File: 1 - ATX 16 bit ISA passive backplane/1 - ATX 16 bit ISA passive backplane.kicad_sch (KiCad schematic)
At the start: 18 parts, among them J1 BUS 1, J2 A: Component Side, J22 IE12, J23 IE23, J24 IE34, J25 IE45, J26 IE56, J27 IE67, J28 IE78, J3 B: Back Side, J4 BUS 2, J5 BUS 3, J6 BUS 4, J7 BUS 5, J8 BUS 6, J9 BUS 7

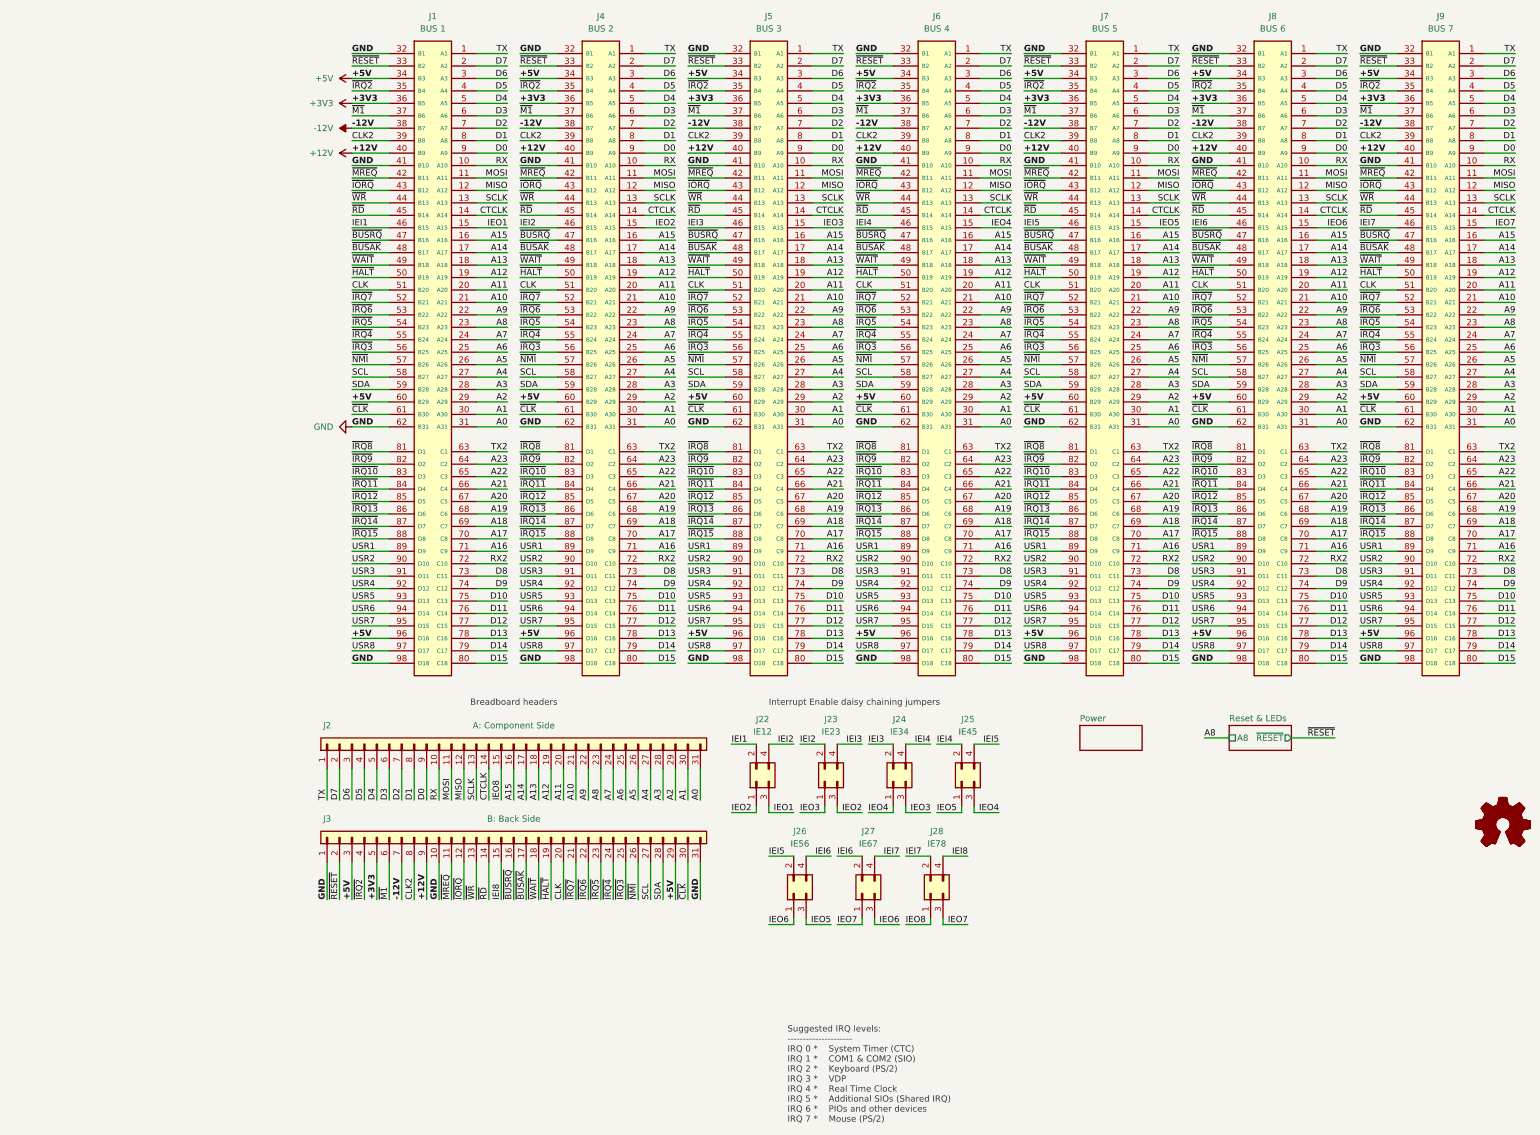
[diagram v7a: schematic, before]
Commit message: Changed lane labeling for IRQ0 and 1
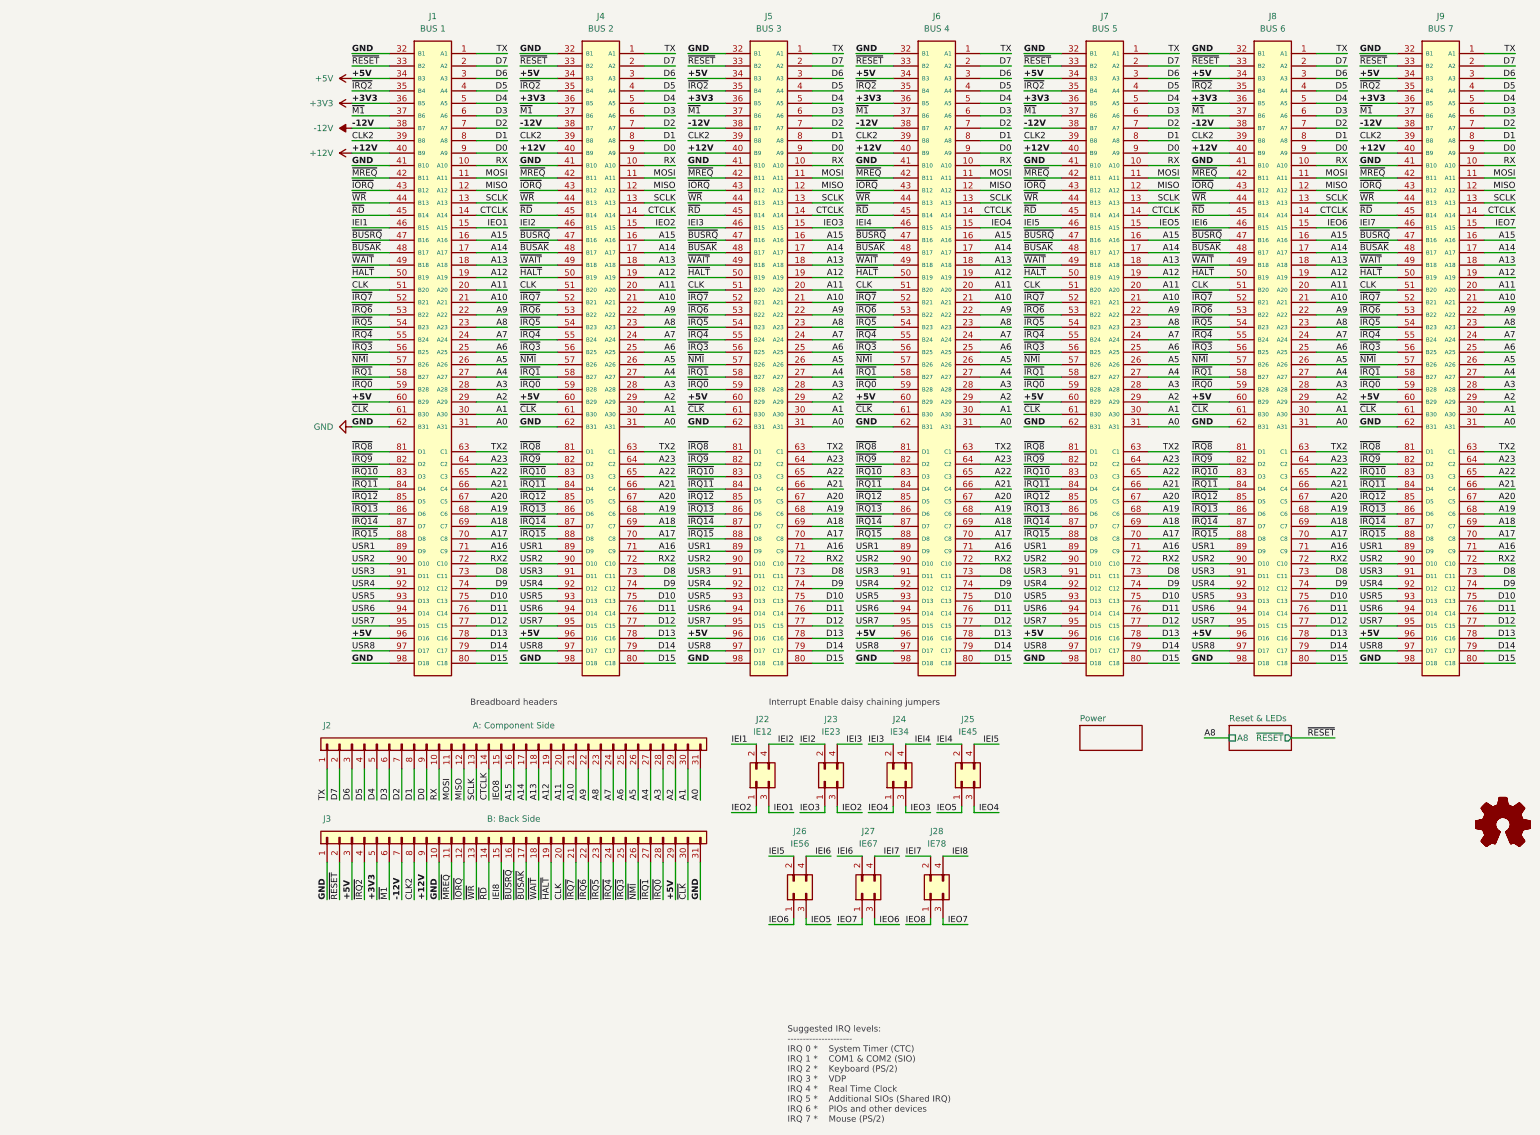
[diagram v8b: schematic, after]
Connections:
- net SCL renamed ~{IRQ1}
- net SDA renamed ~{IRQ0}
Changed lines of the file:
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@@
     (effects (font (size 1.27 1.27)) (justify right bottom))
   )
-  (label "SCL" (at 229.87 88.9 0) (fields_autoplaced)
+  (label "~{IRQ1}" (at 229.87 88.9 0) (fields_autoplaced)
     (effects (font (size 1.27 1.27)) (justify left bottom))
   )
@@
     (effects (font (size 1.27 1.27)) (justify right bottom))
   )
-  (label "SCL" (at 161.29 88.9 0) (fields_autoplaced)
+  (label "~{IRQ1}" (at 161.29 88.9 0) (fields_autoplaced)
     (effects (font (size 1.27 1.27)) (justify left bottom))
   )
@@
     (effects (font (size 1.27 1.27)) (justify right bottom))
   )
-  (label "SDA" (at 24.13 91.44 0) (fields_autoplaced)
+  (label "~{IRQ0}" (at 24.13 91.44 0) (fields_autoplaced)
     (effects (font (size 1.27 1.27)) (justify left bottom))
   )
@@
     (effects (font (size 1.27 1.27)) (justify right bottom))
   )
-  (label "SCL" (at 24.13 88.9 0) (fields_autoplaced)
+  (label "~{IRQ1}" (at 24.13 88.9 0) (fields_autoplaced)
     (effects (font (size 1.27 1.27)) (justify left bottom))
   )
@@
     (effects (font (size 1.27 1.27)) (justify right bottom))
   )
-  (label "SCL" (at 85.09 195.58 90) (fields_autoplaced)
+  (label "~{IRQ1}" (at 85.09 195.58 90) (fields_autoplaced)
     (effects (font (size 1.27 1.27)) (justify left bottom))
   )
@@
     (effects (font (size 1.27 1.27) (thickness 0.254) bold) (justify left bottom))
   )
-  (label "SDA" (at 127 91.44 0) (fields_autoplaced)
+  (label "~{IRQ0}" (at 127 91.44 0) (fields_autoplaced)
     (effects (font (size 1.27 1.27)) (justify left bottom))
   )
@@
     (effects (font (size 1.27 1.27)) (justify right bottom))
   )
-  (label "SDA" (at 87.63 195.58 90) (fields_autoplaced)
+  (label "~{IRQ0}" (at 87.63 195.58 90) (fields_autoplaced)
     (effects (font (size 1.27 1.27)) (justify left bottom))
   )
@@
     (effects (font (size 1.27 1.27)) (justify left bottom))
   )
-  (label "SDA" (at 161.29 91.44 0) (fields_autoplaced)
+  (label "~{IRQ0}" (at 161.29 91.44 0) (fields_autoplaced)
     (effects (font (size 1.27 1.27)) (justify left bottom))
   )
@@
     (effects (font (size 1.27 1.27)) (justify right bottom))
   )
-  (label "SDA" (at 195.58 91.44 0) (fields_autoplaced)
+  (label "~{IRQ0}" (at 195.58 91.44 0) (fields_autoplaced)
     (effects (font (size 1.27 1.27)) (justify left bottom))
   )
@@
     (effects (font (size 1.27 1.27)) (justify left bottom))
   )
-  (label "SDA" (at 58.42 91.44 0) (fields_autoplaced)
+  (label "~{IRQ0}" (at 58.42 91.44 0) (fields_autoplaced)
     (effects (font (size 1.27 1.27)) (justify left bottom))
   )
@@
     (effects (font (size 1.27 1.27)) (justify right bottom))
   )
-  (label "SDA" (at 92.71 91.44 0) (fields_autoplaced)
+  (label "~{IRQ0}" (at 92.71 91.44 0) (fields_autoplaced)
     (effects (font (size 1.27 1.27)) (justify left bottom))
   )
@@
     (effects (font (size 1.27 1.27)) (justify left bottom))
   )
-  (label "SCL" (at 58.42 88.9 0) (fields_autoplaced)
+  (label "~{IRQ1}" (at 58.42 88.9 0) (fields_autoplaced)
     (effects (font (size 1.27 1.27)) (justify left bottom))
   )
@@
     (effects (font (size 1.27 1.27)) (justify left bottom))
   )
-  (label "SDA" (at 229.87 91.44 0) (fields_autoplaced)
+  (label "~{IRQ0}" (at 229.87 91.44 0) (fields_autoplaced)
     (effects (font (size 1.27 1.27)) (justify left bottom))
   )
@@
     (effects (font (size 1.27 1.27)) (justify left bottom))
   )
-  (label "SCL" (at 92.71 88.9 0) (fields_autoplaced)
+  (label "~{IRQ1}" (at 92.71 88.9 0) (fields_autoplaced)
     (effects (font (size 1.27 1.27)) (justify left bottom))
   )
@@
     (effects (font (size 1.27 1.27)) (justify left bottom))
   )
-  (label "SCL" (at 127 88.9 0) (fields_autoplaced)
+  (label "~{IRQ1}" (at 127 88.9 0) (fields_autoplaced)
     (effects (font (size 1.27 1.27)) (justify left bottom))
   )
@@
     (effects (font (size 1.27 1.27)) (justify left bottom))
   )
-  (label "SCL" (at 195.58 88.9 0) (fields_autoplaced)
-    (effects (font (size 1.27 1.27)) (justify left bottom))
-  )
+  (label "~{IRQ1}" (at 195.58 88.9 0) (fields_autoplaced)
+    (effects (font (size 1.27 1.27)) (justify left bottom))
+  )
